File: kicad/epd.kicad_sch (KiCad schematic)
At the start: 24 parts, among them Q501 SI1308EDL

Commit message: refactor, fix issues, ready for first design
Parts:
- removed JP501: BS_L_JP, symbol Jumper:SolderJumper_3_Bridged12
- removed JP502: RESE_JP, symbol Jumper:SolderJumper_3_Bridged12
- added JP401: BS_L_JP, symbol Jumper:SolderJumper_3_Open
- added JP402: RESE_JP, symbol Jumper:SolderJumper_3_Open
- added R407, R408: 100k, symbol Device:R
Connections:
- net BS: now also JP401.2 (C)
- net GND: now also JP401.1 (A), JP402.2 (C)
- net PWR: now also JP401.3 (B), R407.1, R408.1
- net at R503.1: now also JP402.1 (A)
- net at R502.1: now also JP402.3 (B)
- net CS renamed CS_N
- net CS_N: now also R407.2
- net RES renamed RES_N
- net RES_N: now also R408.2
- net SCL renamed SCK
- net SDA renamed MOSI
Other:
- note added: "1 IS DEFAULT"
- note added: "3-line (PWR): No CS/MISO 4-line (GND, DEFAULT): CS/MISO"
- note removed: "3-line (PWR): No CS/MISO 4-line (GND, default): CS/MISO"
- moved on the sheet: EPD_FPC501

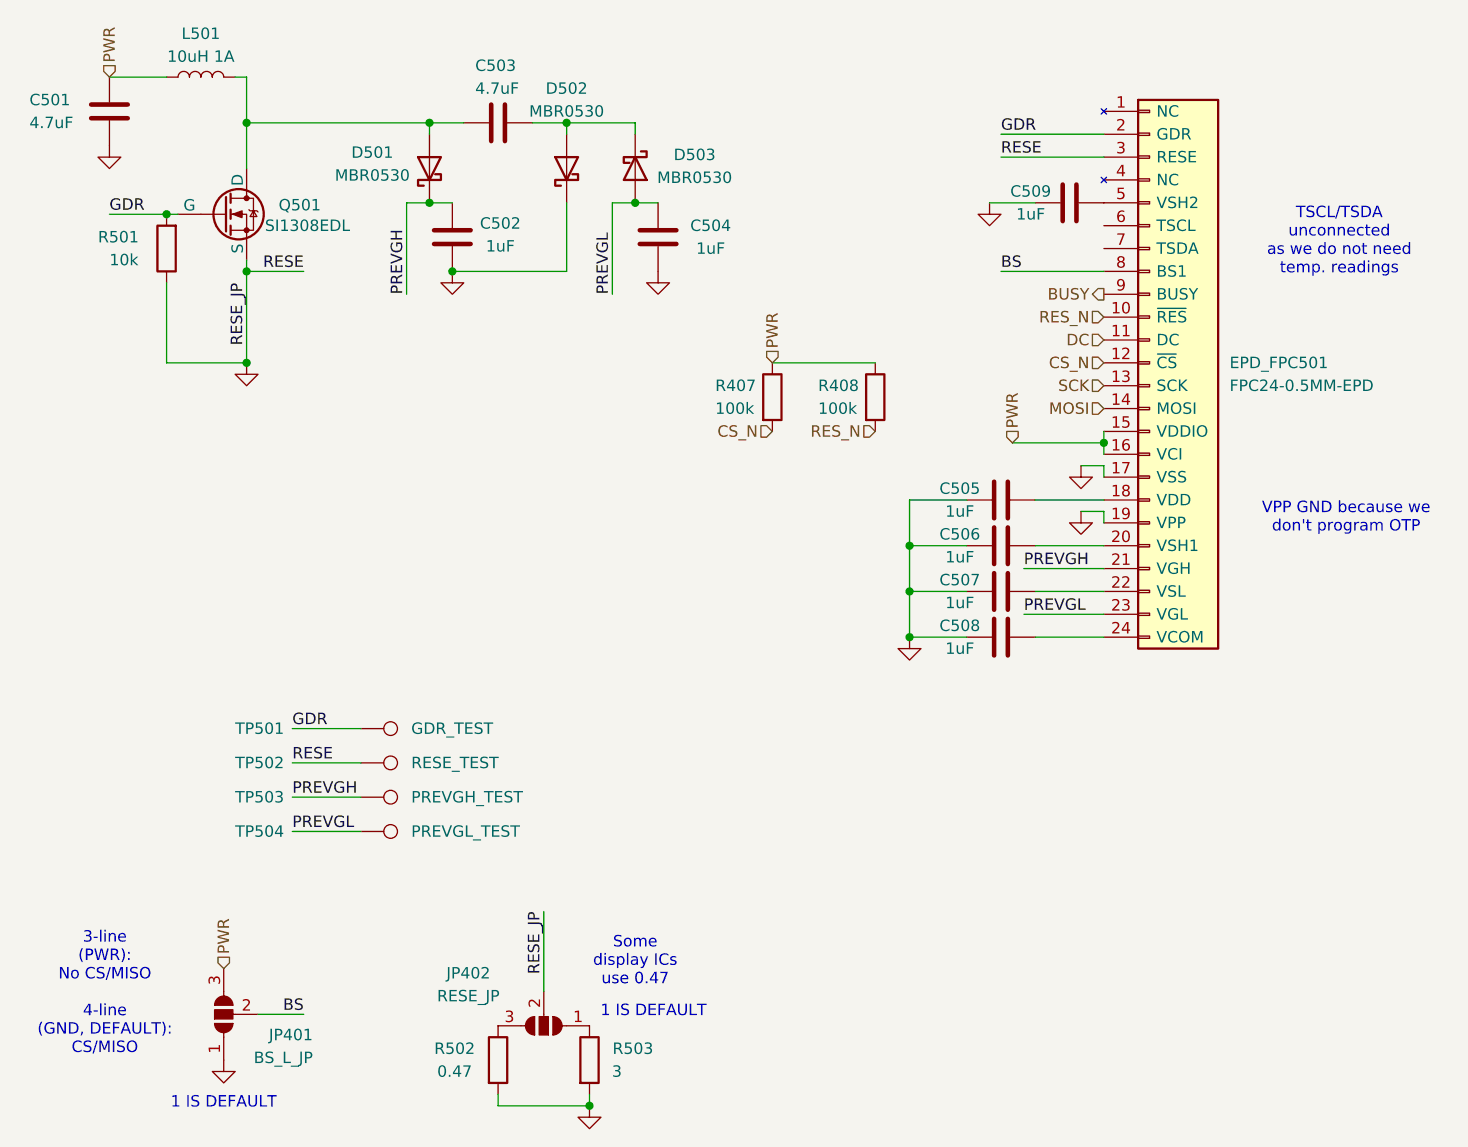
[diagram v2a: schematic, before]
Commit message: essentially finish schematic, start adding footprints, add new footprints
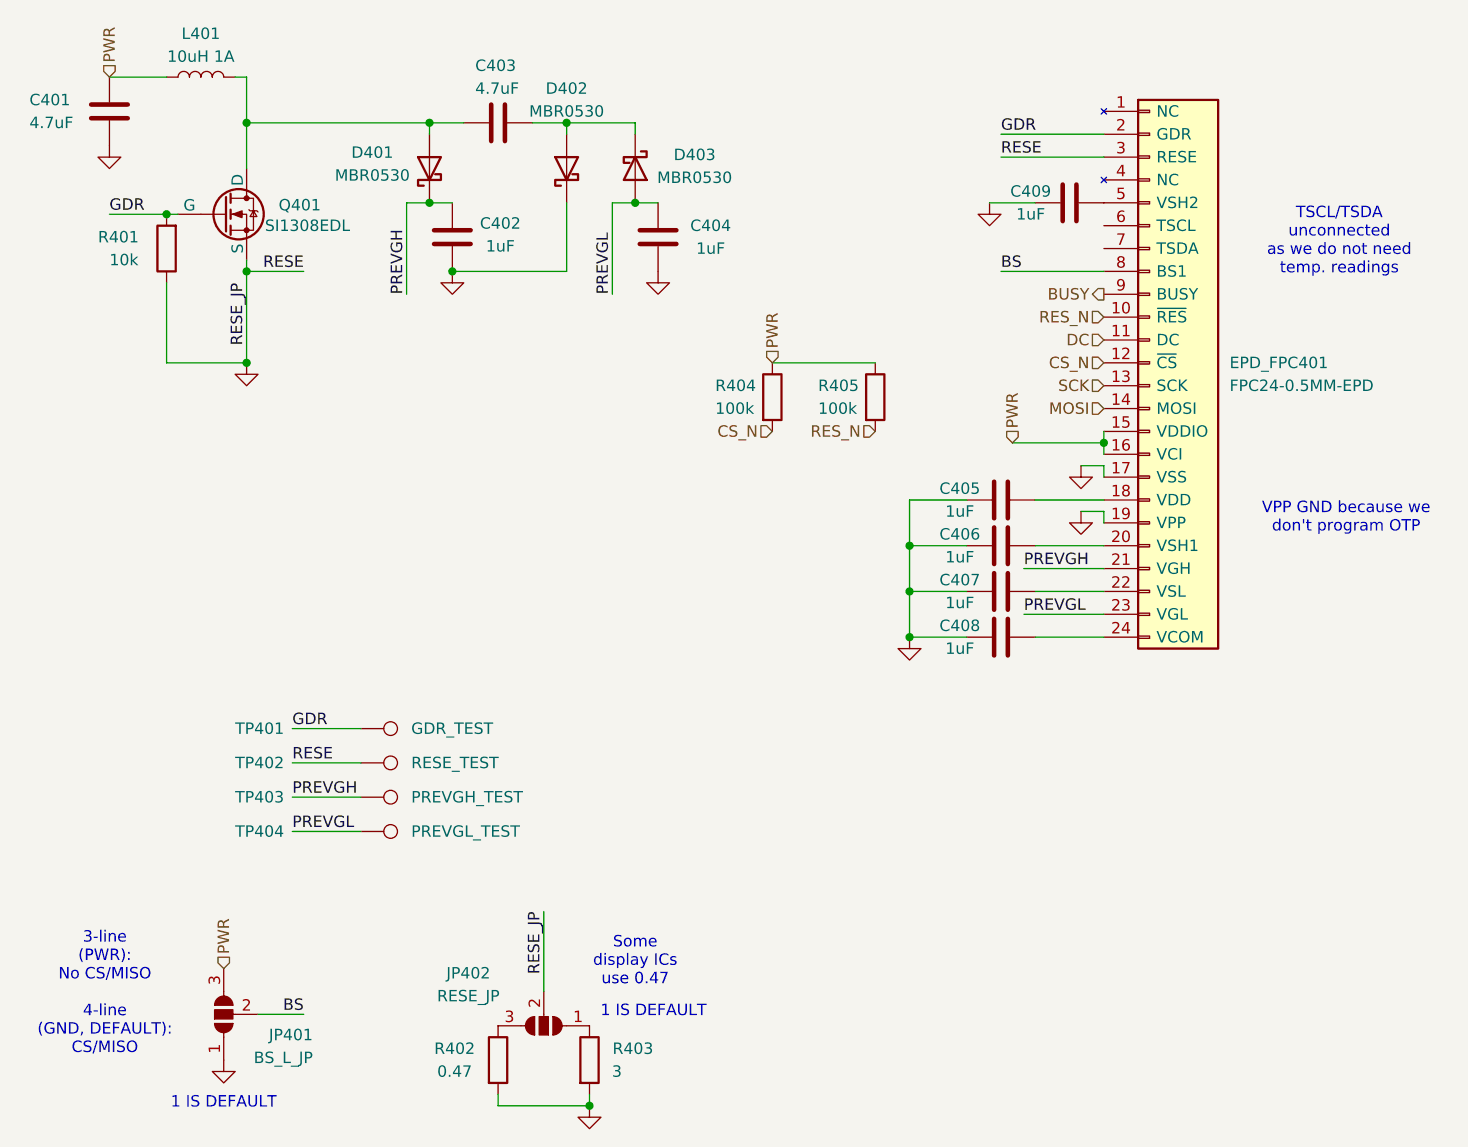
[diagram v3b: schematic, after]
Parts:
- C401: renamed from C501; footprint (none) -> Capacitor_SMD:C_0805_2012Metric_Pad1.18x1.45mm_HandSolder
- C402: renamed from C502; footprint (none) -> Capacitor_SMD:C_0805_2012Metric_Pad1.18x1.45mm_HandSolder
- C403: renamed from C503; footprint (none) -> Capacitor_SMD:C_0805_2012Metric_Pad1.18x1.45mm_HandSolder
- C404: renamed from C504; footprint (none) -> Capacitor_SMD:C_0805_2012Metric_Pad1.18x1.45mm_HandSolder
- C405: renamed from C505; footprint (none) -> Capacitor_SMD:C_0805_2012Metric_Pad1.18x1.45mm_HandSolder
- C406: renamed from C506; footprint (none) -> Capacitor_SMD:C_0805_2012Metric_Pad1.18x1.45mm_HandSolder
- C407: renamed from C507; footprint (none) -> Capacitor_SMD:C_0805_2012Metric_Pad1.18x1.45mm_HandSolder
- C408: renamed from C508; footprint (none) -> Capacitor_SMD:C_0805_2012Metric_Pad1.18x1.45mm_HandSolder
- C409: renamed from C509; footprint (none) -> Capacitor_SMD:C_0805_2012Metric_Pad1.18x1.45mm_HandSolder
- JP401, JP402: footprint (none) -> Jumper:SolderJumper-3_P2.0mm_Open_TrianglePad1.0x1.5mm_NumberLabels
- Q401: renamed from Q501; footprint (none) -> Diode_SMD:D_SOD-323_HandSoldering
- R401: renamed from R501; footprint (none) -> Resistor_SMD:R_0603_1608Metric_Pad0.98x0.95mm_HandSolder
- R402: renamed from R502; footprint (none) -> Resistor_SMD:R_0603_1608Metric_Pad0.98x0.95mm_HandSolder
- R403: renamed from R503; footprint (none) -> Resistor_SMD:R_0603_1608Metric_Pad0.98x0.95mm_HandSolder
- R404: renamed from R407; footprint (none) -> Resistor_SMD:R_0603_1608Metric_Pad0.98x0.95mm_HandSolder
- R405: renamed from R408; footprint (none) -> Resistor_SMD:R_0603_1608Metric_Pad0.98x0.95mm_HandSolder
- TP401: renamed from TP501; footprint (none) -> TestPoint:TestPoint_Pad_D3.0mm
- TP402: renamed from TP502; footprint (none) -> TestPoint:TestPoint_Pad_D3.0mm
- TP403: renamed from TP503; footprint (none) -> TestPoint:TestPoint_Pad_D3.0mm
- TP404: renamed from TP504; footprint (none) -> TestPoint:TestPoint_Pad_D3.0mm
- renumbered D501 to D401, D502 to D402, D503 to D403, EPD_FPC501 to EPD_FPC401, L501 to L401

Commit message: fix motor with spring fingers, start PCB
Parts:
- EPD_FPC401: footprint (none) -> Raven:CONN24x1_FH34SRJ-24S-0.5SH50_HIR
- L401: footprint (none) -> Raven:IND_BOURNS_SRN3015
- TP401, TP402, TP403, TP404: footprint TestPoint:TestPoint_Pad_D3.0mm -> TestPoint:TestPoint_Pad_D1.5mm
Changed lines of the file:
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@@
 			)
 		)
-		(property "Footprint" "TestPoint:TestPoint_Pad_D3.0mm"
+		(property "Footprint" "TestPoint:TestPoint_Pad_D1.5mm"
 			(at 109.22 123.19 0)
 			(effects
@@
 			)
 		)
-		(property "Footprint" "TestPoint:TestPoint_Pad_D3.0mm"
+		(property "Footprint" "TestPoint:TestPoint_Pad_D1.5mm"
 			(at 109.22 125.73 0)
 			(effects
@@
 			)
 		)
-		(property "Footprint" ""
+		(property "Footprint" "Raven:CONN24x1_FH34SRJ-24S-0.5SH50_HIR"
 			(at 196.85 80.01 0)
 			(effects
@@
 			)
 		)
-		(property "Footprint" "TestPoint:TestPoint_Pad_D3.0mm"
+		(property "Footprint" "TestPoint:TestPoint_Pad_D1.5mm"
 			(at 109.22 127 0)
 			(effects
@@
 			)
 		)
-		(property "Footprint" ""
+		(property "Footprint" "Raven:IND_BOURNS_SRN3015"
 			(at 91.44 48.26 0)
 			(effects
@@
 			)
 		)
-		(property "Footprint" "TestPoint:TestPoint_Pad_D3.0mm"
+		(property "Footprint" "TestPoint:TestPoint_Pad_D1.5mm"
 			(at 109.22 129.54 0)
 			(effects

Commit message: fix errors/update USB-c footprint, DA7280 footprint still needs fixing
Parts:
- Q401: footprint Diode_SMD:D_SOD-323_HandSoldering -> Package_TO_SOT_SMD:SOT-323_SC-70_Handsoldering
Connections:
- new net: EPD_FPC401.25 (MNT_NC), EPD_FPC401.26 (MNT_NC)
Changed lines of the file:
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@@
 			)
 		)
-		(property "Footprint" "Diode_SMD:D_SOD-323_HandSoldering"
+		(property "Footprint" "Package_TO_SOT_SMD:SOT-323_SC-70_Handsoldering"
 			(at 99.06 60.96 0)
 			(effects
@@
 		(pin "20"
 		)
-		(instances
+		(pin "25"
+		)
+		(pin "26"
+		)
+		(instances

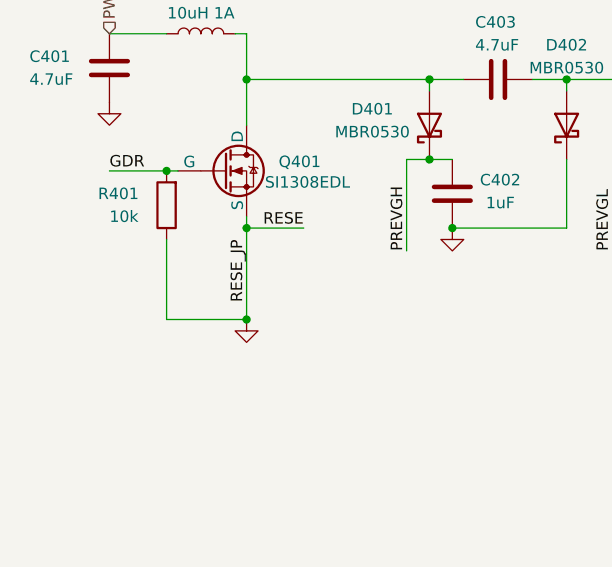
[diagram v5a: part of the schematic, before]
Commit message: PCB almost finished: only battery & usb-c needed
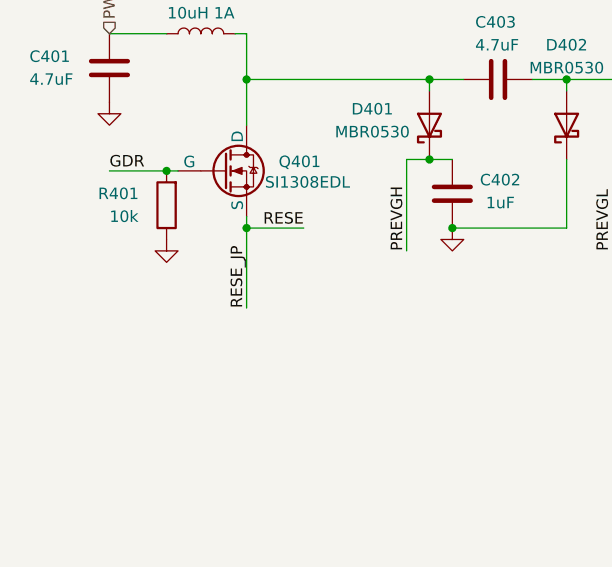
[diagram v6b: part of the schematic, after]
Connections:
- net GND: no longer EPD_FPC401.3 (RESE), JP402.2 (C), Q401.3 (S), TP402.1
- new net RESE: EPD_FPC401.3 (RESE), JP402.2 (C), Q401.3 (S), TP402.1
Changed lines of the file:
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@@
+	)
+	(junction
+		(at 96.52 69.85)
+		(diameter 0)
+		(color 0 0 0 0)
 	)
 	(junction
@@
 	)
 	(junction
-		(at 96.52 69.85)
-		(diameter 0)
-		(color 0 0 0 0)
-	)
-	(junction
 		(at 116.84 53.34)
 		(diameter 0)
@@
 	)
 	(junction
-		(at 96.52 80.01)
-		(diameter 0)
-		(color 0 0 0 0)
-	)
-	(junction
 		(at 139.7 62.23)
 		(diameter 0)
@@
 	(wire
 		(pts
+			(xy 96.52 69.85) (xy 96.52 78.74)
+		)
+		(stroke
+			(width 0)
+			(type default)
+		)
+	)
+	(wire
+		(pts
 			(xy 81.28 48.26) (xy 87.63 48.26)
 		)
@@
 	(wire
 		(pts
-			(xy 96.52 69.85) (xy 96.52 80.01)
-		)
-		(stroke
-			(width 0)
-			(type default)
-		)
-	)
-	(wire
-		(pts
 			(xy 170.18 95.25) (xy 170.18 100.33)
 		)
@@
 	(wire
 		(pts
-			(xy 87.63 71.12) (xy 87.63 80.01)
-		)
-		(stroke
-			(width 0)
-			(type default)
-		)
-	)
-	(wire
-		(pts
 			(xy 119.38 69.85) (xy 132.08 69.85)
 		)
@@
 		(pts
 			(xy 124.46 162.56) (xy 124.46 161.29)
-		)
-		(stroke
-			(width 0)
-			(type default)
-		)
-	)
-	(wire
-		(pts
-			(xy 87.63 80.01) (xy 96.52 80.01)
 		)
 		(stroke
@@
 	)
 	(label "RESE_JP"
-		(at 96.52 71.12 270)
-		(fields_autoplaced yes)
-		(effects
-			(font
-				(size 1.27 1.27)
-			)
-			(justify right bottom)
+		(at 96.52 78.74 90)
+		(fields_autoplaced yes)
+		(effects
+			(font
+				(size 1.27 1.27)
+			)
+			(justify left bottom)
 		)
 	)
@@
 	(symbol
 		(lib_id "power:GND")
-		(at 96.52 80.01 0)
+		(at 87.63 71.12 0)
 		(unit 1)
 		(exclude_from_sim no)
@@
 		(fields_autoplaced yes)
 		(property "Reference" "#PWR0403"
-			(at 96.52 86.36 0)
+			(at 87.63 77.47 0)
 			(effects
 				(font
@@
 		)
 		(property "Value" "GND"
-			(at 96.52 85.09 0)
+			(at 87.63 76.2 0)
 			(effects
 				(font
@@
 		)
 		(property "Footprint" ""
-			(at 96.52 80.01 0)
+			(at 87.63 71.12 0)
 			(effects
 				(font
@@
 		)
 		(property "Datasheet" ""
-			(at 96.52 80.01 0)
+			(at 87.63 71.12 0)
 			(effects
 				(font
@@
 		)
 		(property "Description" "Power symbol creates a global label with name \"GND\" , ground"
-			(at 96.52 80.01 0)
-			(effects
-				(font
+			(at 87.63 71.12 0)
+			(effects
+				(font

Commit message: add some assembly files, but transition towards all hand
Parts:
- C401, C403, D401, D402, D403, EPD_FPC401, JP401, JP402, L401, Q401, R402, R403, TP401, TP402, TP403, TP404: JLC (none) -> XXXXXX; LCSC (none) -> XXXXXX
- C402, C404, C405, C406, C407, C408, C409: JLC (none) -> 0805
- R401, R404, R405: JLC (none) -> 0603

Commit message: new battery management w/ separate LDO/charger almost done
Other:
- company: Author: Lucas Merritt -> Mosaic Labs
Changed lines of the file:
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@@
 		(date "2024-09-03")
 		(rev "1")
-		(company "Author: Lucas Merritt")
+		(company "Mosaic Labs")
+		(comment 1 "Lucas Merritt")
 	)
 	(junction
